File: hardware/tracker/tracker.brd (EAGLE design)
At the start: 69 x 39 mm, 2 parts, among them X1 MINI-USB-SHIELD-UX60-MB-5ST

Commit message: Parts libraries started
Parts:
- added U$2: BMP085, bmp085:BMP085
- added U$3: CC2540-MINI-BLE, cc2540:CC2540-MINI-BLE
- X1: value MINI-USB-SHIELD-UX60-MB-5ST -> MINI-USB-SCHIELD-32005-301; device con-hirose:UX60-MB-5ST -> con-cypressindustries:32005-301
- moved X1 7.13 mm to (5.00, 8.00)
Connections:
- new net +5V: X1.1
- new net GND: U$2.P$1, U$3.P$02, X1.5, X1.M1, X1.M2, X1.M3, X1.M4
- new net VCC: U$3.P$03
- new net VDDA: U$2.P$3
- new net VDDD: U$2.P$4
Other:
- board size 69 x 39 mm -> 69 x 65 mm
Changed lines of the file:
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@@
 <layer number="43" name="vRestrict" color="2" fill="10" visible="yes" active="yes"/>
 <layer number="44" name="Drills" color="7" fill="1" visible="no" active="yes"/>
-<layer number="45" name="Holes" color="7" fill="1" visible="no" active="yes"/>
+<layer number="45" name="Holes" color="7" fill="1" visible="yes" active="yes"/>
 <layer number="46" name="Milling" color="3" fill="1" visible="no" active="yes"/>
 <layer number="47" name="Measures" color="7" fill="1" visible="no" active="yes"/>
@@
 <plain>
 <wire x1="0" y1="0" x2="69" y2="0" width="0" layer="20"/>
-<wire x1="69" y1="0" x2="69" y2="39" width="0" layer="20"/>
-<wire x1="69" y1="39" x2="0" y2="39" width="0" layer="20"/>
-<wire x1="0" y1="39" x2="0" y2="0" width="0" layer="20"/>
+<wire x1="69" y1="0" x2="69" y2="65" width="0" layer="20"/>
+<wire x1="69" y1="65" x2="0" y2="65" width="0" layer="20"/>
+<wire x1="0" y1="65" x2="0" y2="0" width="0" layer="20"/>
 </plain>
 <attributes>
@@
 <classes>
 <class number="0" name="default" width="0" drill="0">
+</class>
+<class number="1" name="VCC" width="0.3" drill="0">
+</class>
+<class number="2" name="GND" width="0.5" drill="0">
+</class>
+<class number="3" name="+5V" width="0.5" drill="0">
 </class>
 </classes>
@@
 </autorouter>
 <elements>
-<element name="X1" library="con-hirose" package="UX60-MB-5ST" value="MINI-USB-SHIELD-UX60-MB-5ST" x="8.89" y="13.97">
-<attribute name="OC_NEWARK" value="unknown" x="8.89" y="13.97" size="1.778" layer="27" display="off"/>
-<attribute name="MPN" value="" x="8.89" y="13.97" size="1.778" layer="27" display="off"/>
-<attribute name="MF" value="" x="8.89" y="13.97" size="1.778" layer="27" display="off"/>
-<attribute name="OC_FARNELL" value="unknown" x="8.89" y="13.97" size="1.778" layer="27" display="off"/>
+<element name="U$1" library="adxl345" package="LGA14" value="ADXL345" x="21.13" y="24.89"/>
+<element name="X1" library="con-cypressindustries" package="32005-301" value="MINI-USB-SCHIELD-32005-301" x="5" y="8" smashed="yes">
+<attribute name="OC_NEWARK" value="unknown" x="5" y="8" size="1.778" layer="27" display="off"/>
+<attribute name="MPN" value="" x="5" y="8" size="1.778" layer="27" display="off"/>
+<attribute name="MF" value="" x="5" y="8" size="1.778" layer="27" display="off"/>
+<attribute name="OC_FARNELL" value="unknown" x="5" y="8" size="1.778" layer="27" display="off"/>
 </element>
-<element name="U$1" library="adxl345" package="LGA14" value="ADXL345" x="21.13" y="24.89"/>
+<element name="U$3" library="cc2540" package="CC2540-MINI-BLE" value="CC2540-MINI-BLE" x="16" y="31" rot="R90"/>
+<element name="U$2" library="bmp085" package="BMP085" value="BMP085" x="34" y="16"/>
 </elements>
 <signals>
@@
 <contactref element="U$1" pad="P$5"/>
 </signal>
+<signal name="GND">
+<contactref element="X1" pad="M4"/>
+<contactref element="X1" pad="M1"/>
+<contactref element="X1" pad="M3"/>
+<contactref element="X1" pad="M2"/>
+<contactref element="U$3" pad="P$02"/>
+<contactref element="X1" pad="5"/>
+<contactref element="U$2" pad="P$1"/>
+<wire x1="7.9" y1="12.45" x2="31.841" y2="17.2065" width="0" layer="19" extent="1-1"/>
+<wire x1="2" y1="12.45" x2="7.9" y2="12.45" width="0" layer="19" extent="1-1"/>
+<wire x1="8" y1="6.4" x2="7.9" y2="12.45" width="0" layer="19" extent="1-1"/>
+<wire x1="7.9" y1="3.55" x2="8" y2="6.4" width="0" layer="19" extent="1-1"/>
+<wire x1="2" y1="3.55" x2="7.9" y2="3.55" width="0" layer="19" extent="1-1"/>
+<wire x1="6.45" y1="31" x2="7.9" y2="12.45" width="0" layer="19" extent="1-1"/>
+</signal>
+<signal name="VCC">
+<contactref element="U$3" pad="P$03"/>
+</signal>
+<signal name="+5V">
+<contactref element="X1" pad="1"/>
+</signal>
+<signal name="VDDA">
+<contactref element="U$2" pad="P$3"/>
+</signal>
+<signal name="VDDD">
+<contactref element="U$2" pad="P$4"/>
+</signal>
 </signals>

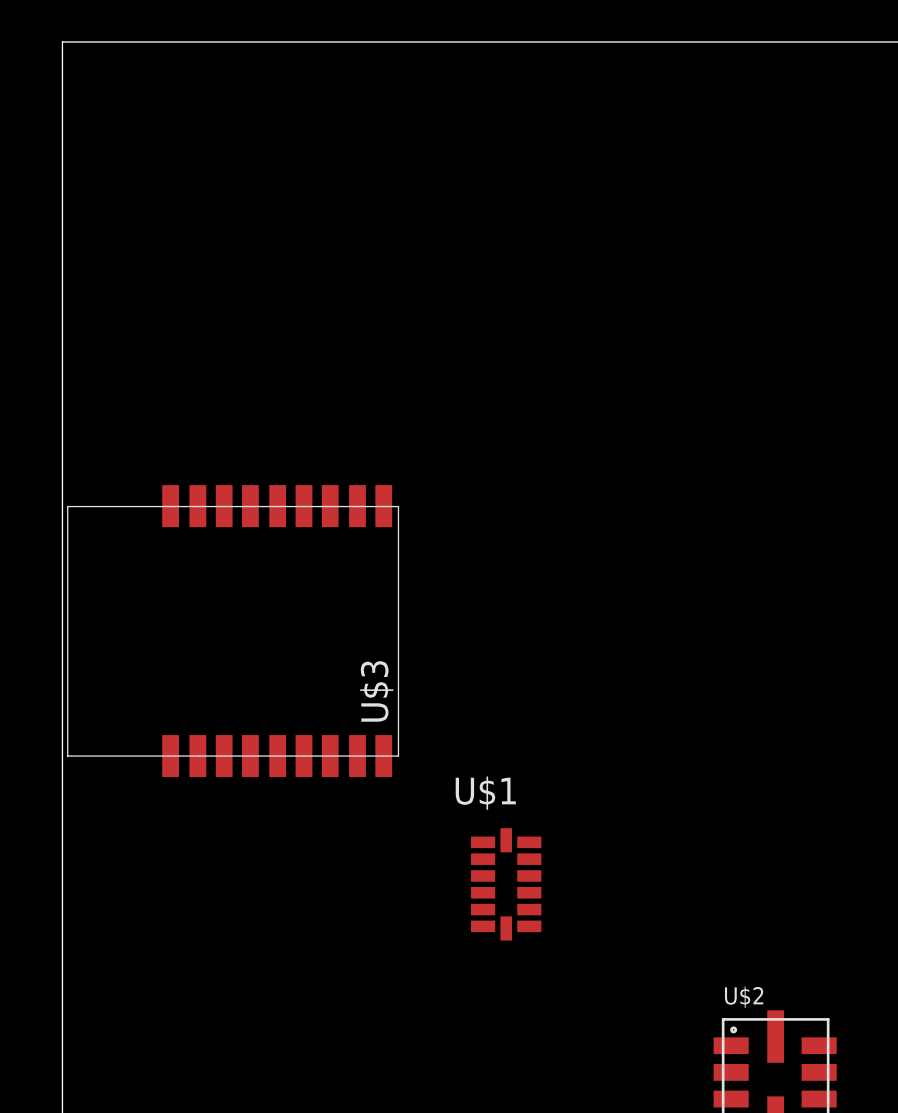
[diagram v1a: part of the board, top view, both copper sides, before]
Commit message: FGPMMOPA6C GPS Standalone Module added
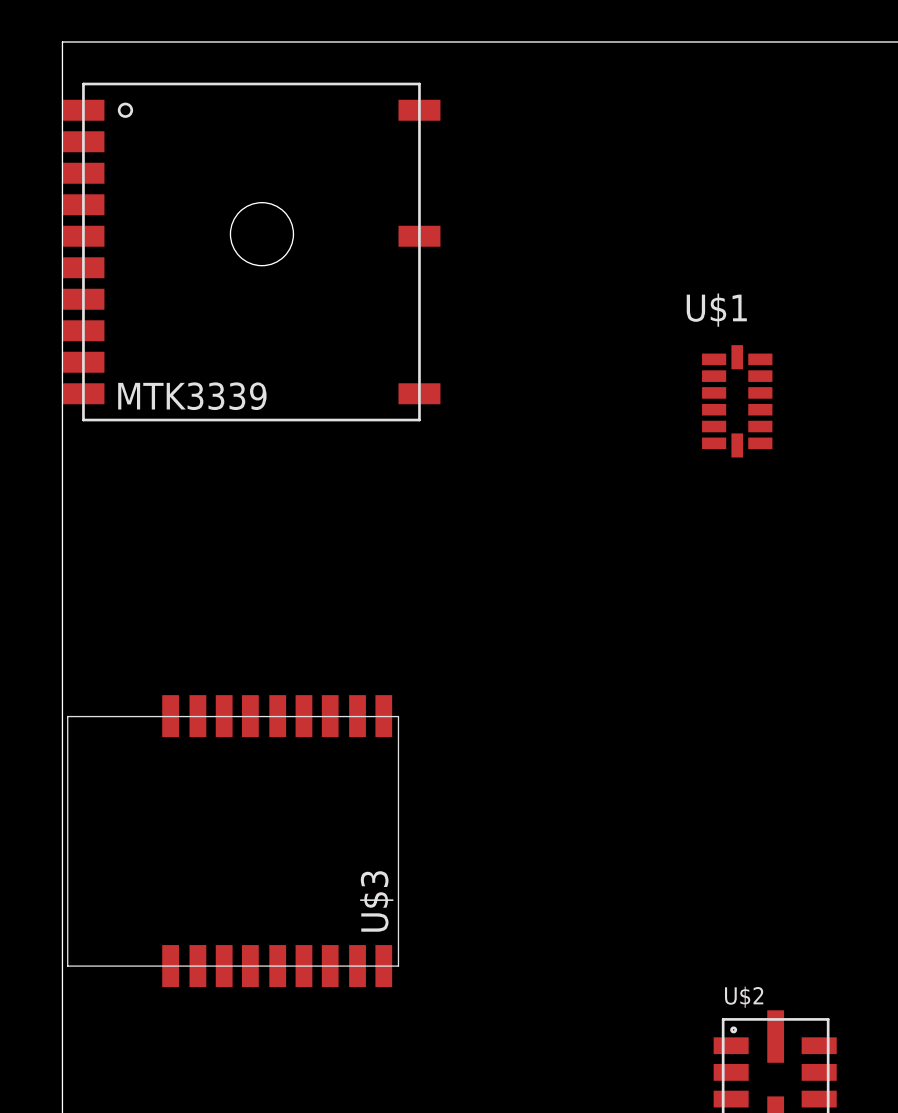
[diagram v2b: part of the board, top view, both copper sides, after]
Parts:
- added U$4: MTK3339, mtk3339:MTK3339
- moved U$1 25.5 mm to (32.1, 47.9)
- moved U$3 10.0 mm to (16.0, 21.0)
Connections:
- new net GND$4: U$4.P$12
- new net GND$5: U$4.P$13
- new net VBACKUP: U$4.P$04
- net GND$1: now also U$4.P$03
- net GND$2: now also U$4.P$08
- net GND$3: now also U$4.P$11
- net VCC: now also U$4.P$01
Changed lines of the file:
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@@
 </autorouter>
 <elements>
-<element name="U$1" library="adxl345" package="LGA14" value="ADXL345" x="21.13" y="24.89"/>
+<element name="U$1" library="adxl345" package="LGA14" value="ADXL345" x="32.13" y="47.89"/>
 <element name="X1" library="con-cypressindustries" package="32005-301" value="MINI-USB-SCHIELD-32005-301" x="5" y="8" smashed="yes">
 <attribute name="OC_NEWARK" value="unknown" x="5" y="8" size="1.778" layer="27" display="off"/>
@@
 <attribute name="OC_FARNELL" value="unknown" x="5" y="8" size="1.778" layer="27" display="off"/>
 </element>
-<element name="U$3" library="cc2540" package="CC2540-MINI-BLE" value="CC2540-MINI-BLE" x="16" y="31" rot="R90"/>
+<element name="U$3" library="cc2540" package="CC2540-MINI-BLE" value="CC2540-MINI-BLE" x="16" y="21" rot="R90"/>
 <element name="U$2" library="bmp085" package="BMP085" value="BMP085" x="34" y="16"/>
+<element name="U$4" library="mtk3339" package="MTK3339" value="MTK3339" x="9" y="55"/>
 </elements>
 <signals>
@@
 <signal name="GND$1">
 <contactref element="U$1" pad="P$2"/>
+<contactref element="U$4" pad="P$03"/>
+<wire x1="31.03" y1="49.09" x2="1" y2="58.75" width="0" layer="19" extent="1-1"/>
 </signal>
 <signal name="GND$2">
 <contactref element="U$1" pad="P$4"/>
+<contactref element="U$4" pad="P$08"/>
+<wire x1="31.03" y1="47.49" x2="1" y2="51.25" width="0" layer="19" extent="1-1"/>
 </signal>
 <signal name="GND$3">
 <contactref element="U$1" pad="P$5"/>
+<contactref element="U$4" pad="P$11"/>
+<wire x1="31.03" y1="46.69" x2="17" y2="48.25" width="0" layer="19" extent="1-1"/>
 </signal>
 <signal name="GND">
@@
 <wire x1="7.9" y1="3.55" x2="8" y2="6.4" width="0" layer="19" extent="1-1"/>
 <wire x1="2" y1="3.55" x2="7.9" y2="3.55" width="0" layer="19" extent="1-1"/>
-<wire x1="6.45" y1="31" x2="7.9" y2="12.45" width="0" layer="19" extent="1-1"/>
+<wire x1="6.45" y1="21" x2="7.9" y2="12.45" width="0" layer="19" extent="1-1"/>
 </signal>
 <signal name="VCC">
 <contactref element="U$3" pad="P$03"/>
+<contactref element="U$4" pad="P$01"/>
+<wire x1="7.7" y1="21" x2="1" y2="61.75" width="0" layer="19" extent="1-1"/>
 </signal>
 <signal name="+5V">
@@
 <contactref element="U$2" pad="P$4"/>
 </signal>
+<signal name="VBACKUP">
+<contactref element="U$4" pad="P$04"/>
+</signal>
+<signal name="GND$4">
+<contactref element="U$4" pad="P$12"/>
+</signal>
+<signal name="GND$5">
+<contactref element="U$4" pad="P$13"/>
+</signal>
 </signals>

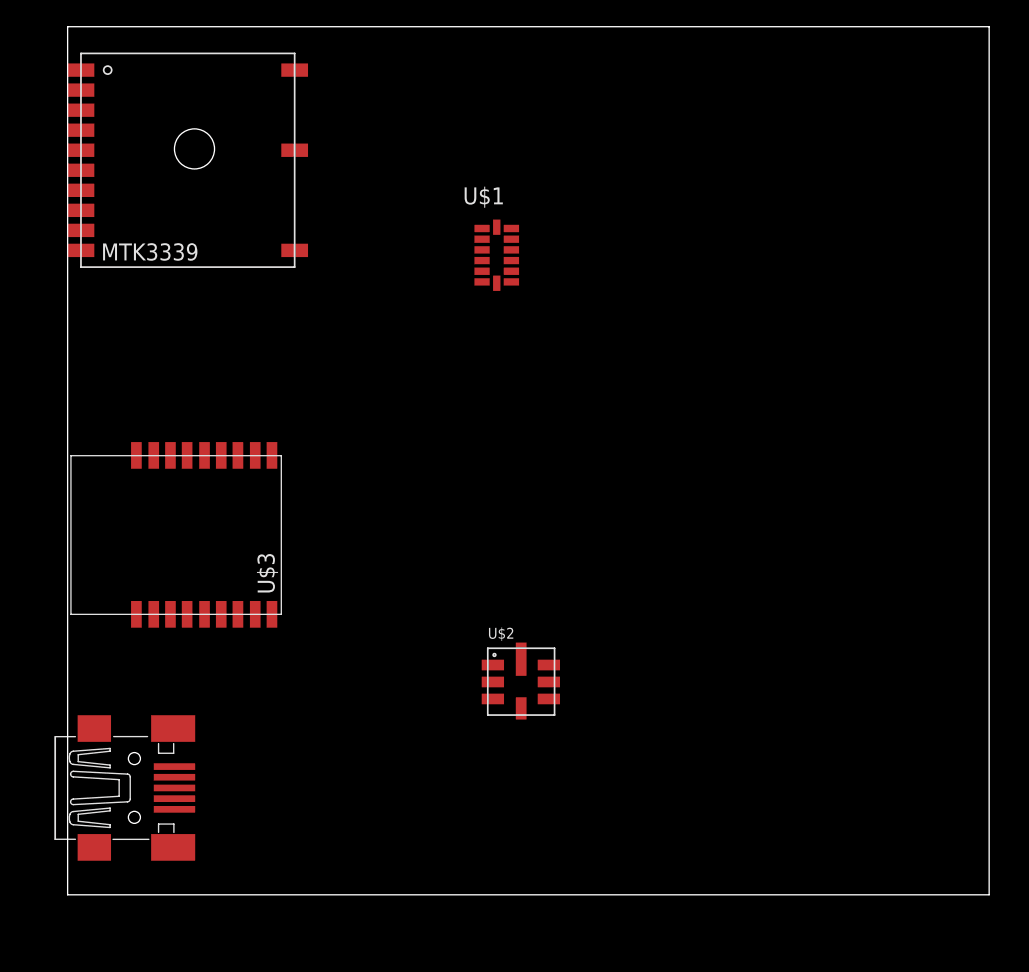
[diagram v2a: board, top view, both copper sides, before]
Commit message: Added KCSA02 and KCSC02 LED modules
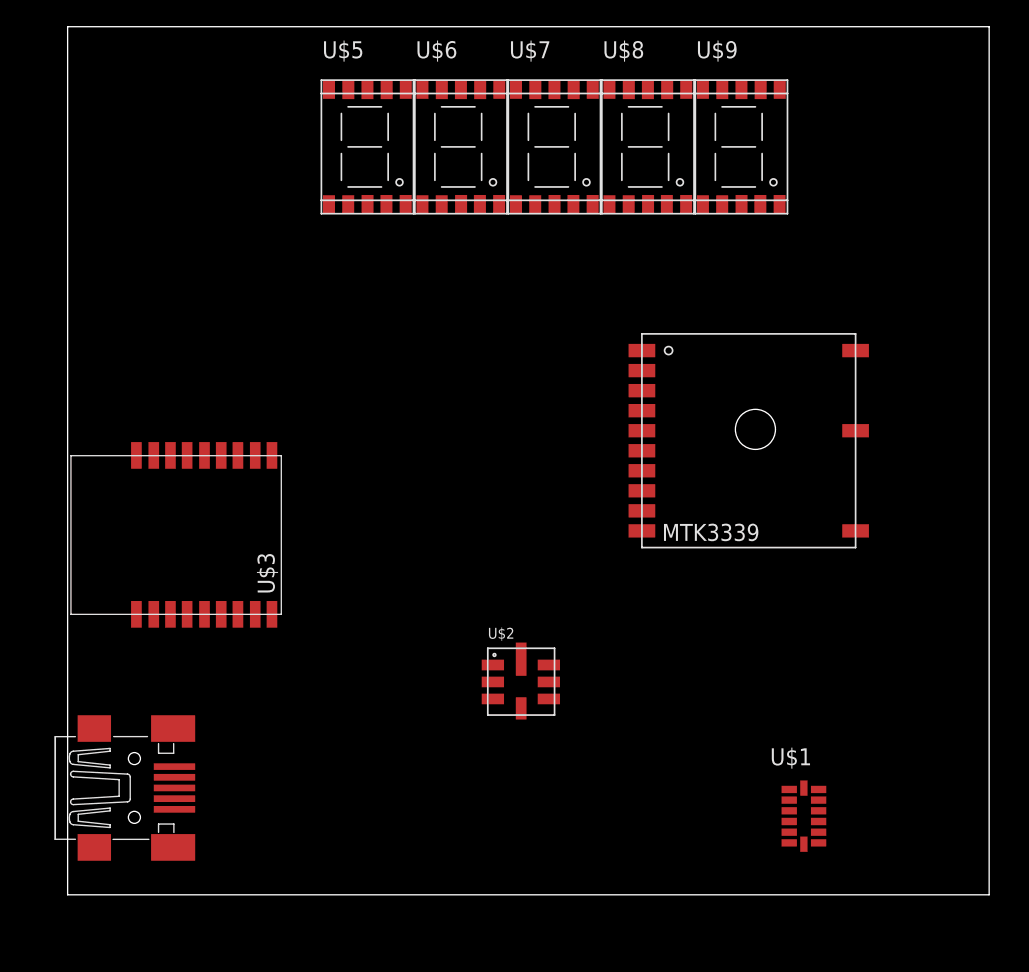
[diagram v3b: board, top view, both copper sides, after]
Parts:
- added U$5, U$6, U$7, U$8, U$9: KCSA02-109-SMALL, kcsx02:KCSX02-SM
- U$4: device mtk3339:MTK3339 -> FGPMMOPA6C:MTK3339
- moved U$1 47.9 mm to (55.1, 5.89)
- moved U$4 47.0 mm to (51.0, 34.0)
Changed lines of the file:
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@@
 </autorouter>
 <elements>
-<element name="U$1" library="adxl345" package="LGA14" value="ADXL345" x="32.13" y="47.89"/>
+<element name="U$1" library="adxl345" package="LGA14" value="ADXL345" x="55.13" y="5.89"/>
 <element name="X1" library="con-cypressindustries" package="32005-301" value="MINI-USB-SCHIELD-32005-301" x="5" y="8" smashed="yes">
 <attribute name="OC_NEWARK" value="unknown" x="5" y="8" size="1.778" layer="27" display="off"/>
@@
 <element name="U$3" library="cc2540" package="CC2540-MINI-BLE" value="CC2540-MINI-BLE" x="16" y="21" rot="R90"/>
 <element name="U$2" library="bmp085" package="BMP085" value="BMP085" x="34" y="16"/>
-<element name="U$4" library="mtk3339" package="MTK3339" value="MTK3339" x="9" y="55"/>
+<element name="U$4" library="FGPMMOPA6C" package="MTK3339" value="MTK3339" x="51" y="34"/>
+<element name="U$5" library="kcsx02" package="KCSX02-SM" value="KCSA02-109-SMALL" x="19" y="51"/>
+<element name="U$6" library="kcsx02" package="KCSX02-SM" value="KCSA02-109-SMALL" x="26" y="51"/>
+<element name="U$7" library="kcsx02" package="KCSX02-SM" value="KCSA02-109-SMALL" x="33" y="51"/>
+<element name="U$8" library="kcsx02" package="KCSX02-SM" value="KCSA02-109-SMALL" x="40" y="51"/>
+<element name="U$9" library="kcsx02" package="KCSX02-SM" value="KCSA02-109-SMALL" x="47" y="51"/>
 </elements>
 <signals>
@@
 <contactref element="U$1" pad="P$2"/>
 <contactref element="U$4" pad="P$03"/>
-<wire x1="31.03" y1="49.09" x2="1" y2="58.75" width="0" layer="19" extent="1-1"/>
+<wire x1="43" y1="37.75" x2="54.03" y2="7.09" width="0" layer="19" extent="1-1"/>
 </signal>
 <signal name="GND$2">
 <contactref element="U$1" pad="P$4"/>
 <contactref element="U$4" pad="P$08"/>
-<wire x1="31.03" y1="47.49" x2="1" y2="51.25" width="0" layer="19" extent="1-1"/>
+<wire x1="43" y1="30.25" x2="54.03" y2="5.49" width="0" layer="19" extent="1-1"/>
 </signal>
 <signal name="GND$3">
 <contactref element="U$1" pad="P$5"/>
 <contactref element="U$4" pad="P$11"/>
-<wire x1="31.03" y1="46.69" x2="17" y2="48.25" width="0" layer="19" extent="1-1"/>
+<wire x1="59" y1="27.25" x2="54.03" y2="4.69" width="0" layer="19" extent="1-1"/>
 </signal>
 <signal name="GND">
@@
 <contactref element="U$3" pad="P$03"/>
 <contactref element="U$4" pad="P$01"/>
-<wire x1="7.7" y1="21" x2="1" y2="61.75" width="0" layer="19" extent="1-1"/>
+<wire x1="43" y1="40.75" x2="7.7" y2="21" width="0" layer="19" extent="1-1"/>
 </signal>
 <signal name="+5V">

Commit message: no message
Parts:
- added BTN1, BTN2: FLAT-BUTTON, ml:FLAT-BUTTON
- added C2, C3, C4: 10uF, resistor:PANASONIC_B
- added D1, D2: (no value), diode:SOD106-R
- added IC1: TP4056, TP4056:SOP-8
- added IC2: LM1117MPX-3.3, lm1117:SOT223
- added R1: PROG, resistor:M0805
- added SW1: PWR-SWITCH, ml:PWR-SWITCH
- added U$10: ADXL345, adxl345:LGA14
- added U$11: CC2540-MINI-BLE, cc2540:CC2540-MINI-BLE
- added U$12: MICROSD, micro-sd:MICROSD
- U$1: value ADXL345 -> KCSA02-109-SMALL; device adxl345:LGA14 -> kcsx02:KCSX02-SM
- U$2: value BMP085 -> KCSA02-109-SMALL; device bmp085:BMP085 -> kcsx02:KCSX02-SM
- U$3: value CC2540-MINI-BLE -> KCSA02-109-SMALL; device cc2540:CC2540-MINI-BLE -> kcsx02:KCSX02-SM
- U$4: value MTK3339 -> KCSA02-109-SMALL; device FGPMMOPA6C:MTK3339 -> kcsx02:KCSX02-SM
- U$6: value KCSA02-109-SMALL -> BATTERY+; device kcsx02:KCSX02-SM -> ml:BATTERY+
- U$7: value KCSA02-109-SMALL -> BATTERY-; device kcsx02:KCSX02-SM -> ml:BATTERY-
- U$8: value KCSA02-109-SMALL -> FGPMMOPA6C; device kcsx02:KCSX02-SM -> FGPMMOPA6C:FGPMMOPA6C
- U$9: value KCSA02-109-SMALL -> BMP085; device kcsx02:KCSX02-SM -> bmp085:BMP085
- moved U$7 48.7 mm to (25.0, 3.00)
- moved U$5 31.8 mm to (41.0, 28.0), turned to 90 degrees
- moved U$8 28.8 mm to (56.0, 27.0), flipped to the bottom, turned to 270 degrees
- moved U$3 26.0 mm to (41.0, 14.0)
- moved U$9 17.0 mm to (64.0, 52.0)
- moved U$4 16.4 mm to (41.0, 21.0), turned to 90 degrees
- moved U$1 15.3 mm to (41.0, 0.00), turned to 90 degrees
- moved U$6 13.6 mm to (37.0, 59.0)
- moved U$2 11.4 mm to (41.0, 7.00), turned to 90 degrees
- moved X1 2.00 mm to (5.00, 6.00)
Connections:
- removed net GND$1: U$1.P$2, U$4.P$03
- removed net GND$2: U$1.P$4, U$4.P$08
- removed net GND$3: U$1.P$5, U$4.P$11
- removed net GND$4: U$4.P$12
- removed net GND$5: U$4.P$13
- new net +3V3: C3.+, IC2.2, IC2.TAB
- new net A: U$1.7, U$2.7, U$3.7, U$4.7, U$5.7
- new net B: U$1.6, U$2.6, U$3.6, U$4.6, U$5.6
- new net BAT+: C2.+, D2.A, IC1.5, U$6.PAD, U$6.PIN
- new net BAT-PROG: IC1.2, R1.2
- new net C: U$1.4, U$2.4, U$3.4, U$4.4, U$5.4
- new net CHARGER_CHARGING: IC1.7
- new net CHARGER_ENABLE: IC1.8
- new net CHARGER_STANDBY: IC1.6
- new net D: U$1.2, U$2.2, U$3.2, U$4.2, U$5.2
- new net E: U$1.1, U$2.1, U$3.1, U$4.1, U$5.1
- new net F: U$1.9, U$2.9, U$3.9, U$4.9, U$5.9
- new net G: U$1.10, U$2.10, U$3.10, U$4.10, U$5.10
- new net H: U$1.5, U$2.5, U$3.5, U$4.5, U$5.5
- new net N$2: U$1.3, U$1.8
- new net N$3: U$2.3, U$2.8
- new net N$4: U$3.3, U$3.8
- new net N$5: U$4.3, U$4.8
- new net N$6: U$5.3, U$5.8
- new net N$7: D1.C, D2.C, SW1.2
- new net N$8: IC2.3, SW1.3
- new net USB+D: X1.3
- new net USB-D: X1.2
- net +5V: now also C4.+, D1.A, IC1.4
- net GND: now also C2.-, C3.-, C4.-, IC1.1, IC1.3, IC2.1, R1.1, SW1.SCREEN@1, SW1.SCREEN@2, SW1.SCREEN@3, U$10.2, U$10.4, U$10.5, U$11.2, U$7.P$1, U$7.P$2, U$7.P$3, U$8.11, U$8.12, U$8.13, U$8.3, U$8.8, U$9.1; no longer U$2.P$1, U$3.P$02
- net VBACKUP: now also U$8.4; no longer U$4.P$04
- net VCC: now also U$11.3, U$8.1; no longer U$3.P$03, U$4.P$01
- net VDDA: now also U$9.3; no longer U$2.P$3
- net VDDD: now also U$9.4; no longer U$2.P$4
- net VDDIO: now also U$10.1; no longer U$1.P$1
- net VS: now also U$10.6; no longer U$1.P$6
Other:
- board size 69 x 65 mm -> 70 x 65 mm
